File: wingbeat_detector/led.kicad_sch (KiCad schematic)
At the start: 7 parts, among them J2 CONN_UMC_JACK_SMD, Q1 MOSFET-N-CH, U6 LED_DRV_50mA

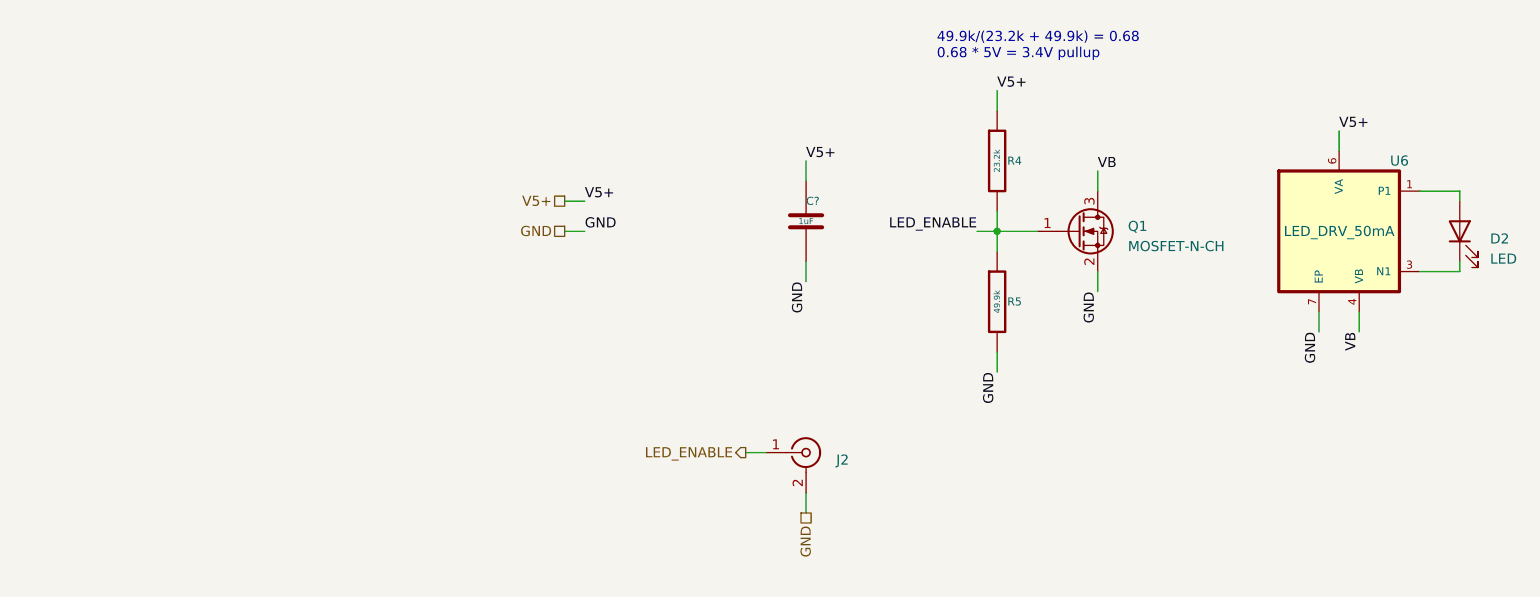
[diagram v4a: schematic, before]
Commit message: Initial schematic layout
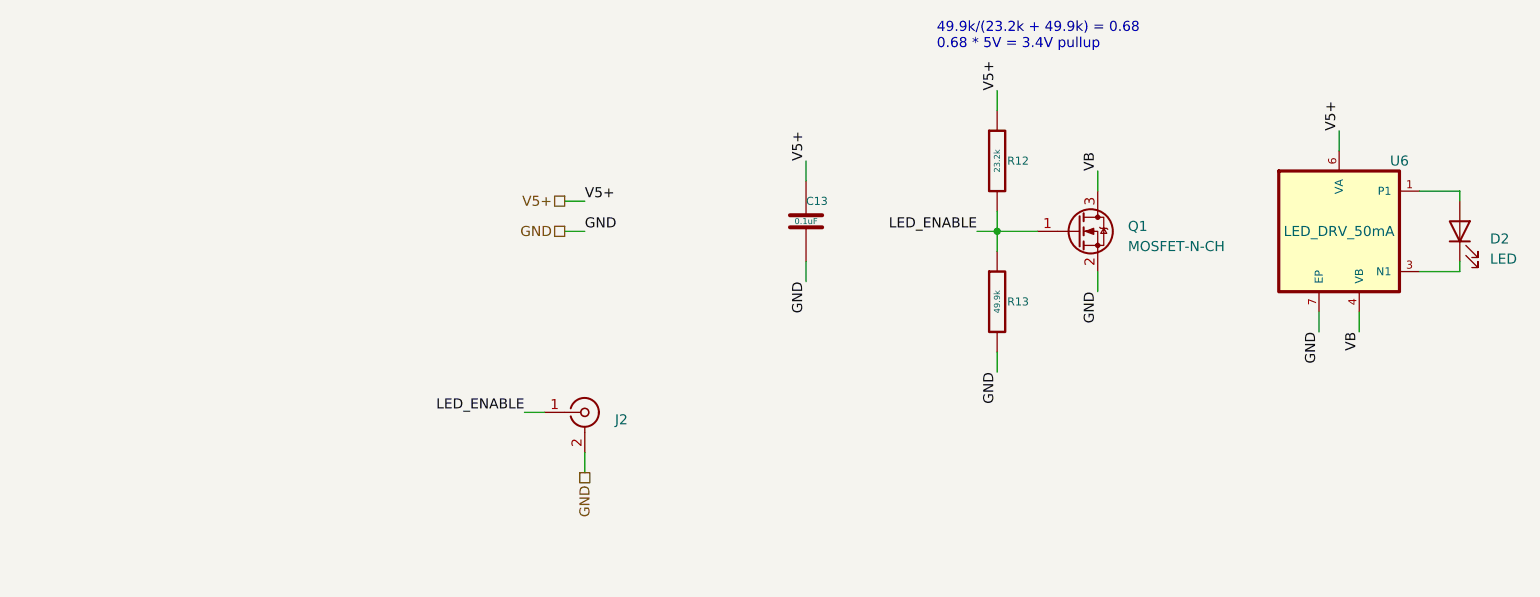
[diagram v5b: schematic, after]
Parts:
- removed C?: 1uF, Janelia:C_0402_1005Metric, symbol Janelia:C_1uF_0402
- added C13: 0.1uF, Janelia:C_0402_1005Metric, symbol Janelia:C_0.1uF_0402
- renumbered R4 to R12, R5 to R13
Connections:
- net GND: now also C13.2
- net V5+: now also C13.1
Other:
- moved on the sheet: J2
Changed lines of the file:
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@@
     (stroke (width 0) (type default))
   )
-  (wire (pts (xy 132.08 121.92) (xy 132.08 124.46))
+  (wire (pts (xy 104.14 116.84) (xy 104.14 119.38))
     (stroke (width 0) (type default))
   )
@@
     (stroke (width 0) (type default))
   )
-  (wire (pts (xy 124.46 116.84) (xy 127 116.84))
+  (wire (pts (xy 96.52 111.76) (xy 99.06 111.76))
     (stroke (width 0) (type default))
   )
@@
   )
   (text "49.9k/(23.2k + 49.9k) = 0.68\n0.68 * 5V = 3.4V pullup"
-    (at 148.59 67.31 0)
-    (effects (font (size 1.27 1.27)) (justify left bottom))
-  )
-  (label "V5+" (at 156.21 71.12 0) (fields_autoplaced)
-    (effects (font (size 1.27 1.27)) (justify left bottom))
-  )
-  (label "V5+" (at 199.39 76.2 0) (fields_autoplaced)
+    (at 148.59 66.04 0)
+    (effects (font (size 1.27 1.27)) (justify left bottom))
+  )
+  (label "V5+" (at 156.21 71.12 90) (fields_autoplaced)
+    (effects (font (size 1.27 1.27)) (justify left bottom))
+  )
+  (label "V5+" (at 199.39 76.2 90) (fields_autoplaced)
     (effects (font (size 1.27 1.27)) (justify left bottom))
   )
@@
     (effects (font (size 1.27 1.27)) (justify right bottom))
   )
+  (label "LED_ENABLE" (at 96.52 111.76 180) (fields_autoplaced)
+    (effects (font (size 1.27 1.27)) (justify right bottom))
+  )
   (label "GND" (at 156.21 106.68 270) (fields_autoplaced)
     (effects (font (size 1.27 1.27)) (justify right bottom))
@@
     (effects (font (size 1.27 1.27)) (justify right bottom))
   )
-  (label "VB" (at 168.91 81.28 0) (fields_autoplaced)
-    (effects (font (size 1.27 1.27)) (justify left bottom))
-  )
-  (label "V5+" (at 132.08 80.01 0) (fields_autoplaced)
+  (label "VB" (at 168.91 81.28 90) (fields_autoplaced)
+    (effects (font (size 1.27 1.27)) (justify left bottom))
+  )
+  (label "V5+" (at 132.08 80.01 90) (fields_autoplaced)
     (effects (font (size 1.27 1.27)) (justify left bottom))
   )
@@
     (effects (font (size 1.27 1.27)) (justify right))
   )
-  (hierarchical_label "LED_ENABLE" (shape output) (at 124.46 116.84 180) (fields_autoplaced)
-    (effects (font (size 1.27 1.27)) (justify right))
-  )
   (hierarchical_label "GND" (shape passive) (at 101.6 88.9 180) (fields_autoplaced)
     (effects (font (size 1.27 1.27)) (justify right))
   )
-  (hierarchical_label "GND" (shape passive) (at 132.08 124.46 270) (fields_autoplaced)
+  (hierarchical_label "GND" (shape passive) (at 104.14 119.38 270) (fields_autoplaced)
     (effects (font (size 1.27 1.27)) (justify right))
-  )
-  (symbol (lib_id "Janelia:C_1uF_0402") (at 132.08 87.63 0) (unit 1)
-    (in_bom yes) (on_board yes) (dnp no)
-    (property "Reference" "C?" (at 132.08 85.09 0)
-      (effects (font (size 1.016 1.016)) (justify left))
-    )
-    (property "Value" "1uF" (at 132.08 87.63 0)
-      (effects (font (size 0.762 0.762)))
-    )
-    (property "Footprint" "Janelia:C_0402_1005Metric" (at 133.0452 91.44 0)
-      (effects (font (size 0.762 0.762)) hide)
-    )
-    (property "Datasheet" "" (at 132.08 87.63 0)
-      (effects (font (size 1.524 1.524)) hide)
-    )
-    (property "Vendor" "Digi-Key" (at 134.62 82.55 0)
-      (effects (font (size 1.524 1.524)) hide)
-    )
-    (property "Vendor Part Number" "1276-6796-1-ND" (at 137.16 80.01 0)
-      (effects (font (size 1.524 1.524)) hide)
-    )
-    (property "Description" "CAP CER 1UF 35V X5R" (at 139.7 77.47 0)
-      (effects (font (size 1.524 1.524)) hide)
-    )
-    (property "Package" "0402" (at 132.08 87.63 0)
-      (effects (font (size 1.27 1.27)) hide)
-    )
-    (property "Manufacturer" "Samsung Electro-Mechanics" (at 132.08 87.63 0)
-      (effects (font (size 1.27 1.27)) hide)
-    )
-    (property "Manufacturer Part Number" "CL05A105KL5NRNC" (at 132.08 87.63 0)
-      (effects (font (size 1.27 1.27)) hide)
-    )
-    (pin "1")
-    (pin "2")
-    (instances
-      (project "wingbeat_detector"
-        (path "/cc457ebc-4af6-4663-b19f-8cb38f061cb4/6f9841bf-b0ef-48ff-bf2c-2bd611c72bf3"
-          (reference "C?") (unit 1)
-        )
-        (path "/cc457ebc-4af6-4663-b19f-8cb38f061cb4/669b71f5-24db-4526-af56-a5891b9eda40"
-          (reference "C9") (unit 1)
-        )
-      )
-    )
   )
   (symbol (lib_id "Janelia:R_23.2k_0402") (at 156.21 80.01 0) (unit 1)
     (in_bom yes) (on_board yes) (dnp no)
-    (property "Reference" "R4" (at 157.48 80.01 0)
+    (property "Reference" "R12" (at 157.48 80.01 0)
       (effects (font (size 1.016 1.016)) (justify left))
     )
@@
       (project "wingbeat_detector"
         (path "/cc457ebc-4af6-4663-b19f-8cb38f061cb4/669b71f5-24db-4526-af56-a5891b9eda40"
-          (reference "R4") (unit 1)
+          (reference "R12") (unit 1)
+        )
+      )
+    )
+  )
+  (symbol (lib_id "Janelia:C_0.1uF_0402") (at 132.08 87.63 0) (unit 1)
+    (in_bom yes) (on_board yes) (dnp no)
+    (property "Reference" "C13" (at 132.08 85.09 0)
+      (effects (font (size 1.016 1.016)) (justify left))
+    )
+    (property "Value" "0.1uF" (at 132.08 87.63 0)
+      (effects (font (size 0.762 0.762)))
+    )
+    (property "Footprint" "Janelia:C_0402_1005Metric" (at 133.0452 91.44 0)
+      (effects (font (size 0.762 0.762)) hide)
+    )
+    (property "Datasheet" "" (at 132.08 87.63 0)
+      (effects (font (size 1.524 1.524)) hide)
+    )
+    (property "Vendor" "Digi-Key" (at 134.62 82.55 0)
+      (effects (font (size 1.524 1.524)) hide)
+    )
+    (property "Vendor Part Number" "311-1375-1-ND" (at 137.16 80.01 0)
+      (effects (font (size 1.524 1.524)) hide)
+    )
+    (property "Description" "CAP CER 0.1UF 25V Y5V" (at 139.7 77.47 0)
+      (effects (font (size 1.524 1.524)) hide)
+    )
+    (property "Package" "0402" (at 132.08 87.63 0)
+      (effects (font (size 1.27 1.27)) hide)
+    )
+    (property "Manufacturer" "Yageo" (at 132.08 87.63 0)
+      (effects (font (size 1.27 1.27)) hide)
+    )
+    (property "Manufacturer Part Number" "CC0402ZRY5V8BB104" (at 132.08 87.63 0)
+      (effects (font (size 1.27 1.27)) hide)
+    )
+    (pin "1")
+    (pin "2")
+    (instances
+      (project "wingbeat_detector"
+        (path "/cc457ebc-4af6-4663-b19f-8cb38f061cb4/669b71f5-24db-4526-af56-a5891b9eda40"
+          (reference "C13") (unit 1)
         )
       )
@@
   (symbol (lib_id "Janelia:R_49.9k_0402") (at 156.21 97.79 0) (unit 1)
     (in_bom yes) (on_board yes) (dnp no)
-    (property "Reference" "R5" (at 157.48 97.79 0)
+    (property "Reference" "R13" (at 157.48 97.79 0)
       (effects (font (size 1.016 1.016)) (justify left))
     )
@@
       (project "wingbeat_detector"
         (path "/cc457ebc-4af6-4663-b19f-8cb38f061cb4/669b71f5-24db-4526-af56-a5891b9eda40"
-          (reference "R5") (unit 1)
+          (reference "R13") (unit 1)
         )
       )
     )
   )
-  (symbol (lib_id "Janelia:CONN_UMC_JACK_SMD") (at 132.08 116.84 0) (unit 1)
+  (symbol (lib_id "Janelia:CONN_UMC_JACK_SMD") (at 104.14 111.76 0) (unit 1)
     (in_bom yes) (on_board yes) (dnp no) (fields_autoplaced)
-    (property "Reference" "J2" (at 135.89 117.7682 0)
+    (property "Reference" "J2" (at 107.95 112.6882 0)
       (effects (font (size 1.27 1.27)) (justify left))
     )
-    (property "Value" "CONN_UMC_JACK_SMD" (at 135.001 116.84 90)
-      (effects (font (size 1.27 1.27)) hide)
-    )
-    (property "Footprint" "Janelia:UMC_AMPHENOL_A-1JB" (at 132.08 104.14 0)
-      (effects (font (size 1.27 1.27)) hide)
-    )
-    (property "Datasheet" "" (at 132.08 116.84 0)
-      (effects (font (size 1.27 1.27)) hide)
-    )
-    (property "Manufacturer" "Amphenol RF" (at 132.08 106.68 0)
-      (effects (font (size 1.27 1.27)) hide)
-    )
-    (property "Manufacturer Part Number" "A-1JB" (at 132.08 132.08 0)
-      (effects (font (size 1.27 1.27)) hide)
-    )
-    (property "Vendor" "Digi-Key" (at 132.08 134.62 0)
-      (effects (font (size 1.27 1.27)) hide)
-    )
-    (property "Vendor Part Number" "115-A-1JBCT-ND" (at 132.08 129.54 0)
-      (effects (font (size 1.27 1.27)) hide)
-    )
-    (property "Description" "CONN UMC JACK STR 50 OHM SMD" (at 132.08 101.6 0)
-      (effects (font (size 1.27 1.27)) hide)
-    )
+    (property "Value" "CONN_UMC_JACK_SMD" (at 107.061 111.76 90)
+      (effects (font (size 1.27 1.27)) hide)
+    )
+    (property "Footprint" "Janelia:UMC_AMPHENOL_A-1JB" (at 104.14 99.06 0)
+      (effects (font (size 1.27 1.27)) hide)
+    )
+    (property "Datasheet" "" (at 104.14 111.76 0)
+      (effects (font (size 1.27 1.27)) hide)
+    )
+    (property "Manufacturer" "Amphenol RF" (at 104.14 101.6 0)
+      (effects (font (size 1.27 1.27)) hide)
+    )
+    (property "Manufacturer Part Number" "A-1JB" (at 104.14 127 0)
+      (effects (font (size 1.27 1.27)) hide)
+    )
+    (property "Vendor" "Digi-Key" (at 104.14 129.54 0)
+      (effects (font (size 1.27 1.27)) hide)
+    )
+    (property "Vendor Part Number" "115-A-1JBCT-ND" (at 104.14 124.46 0)
+      (effects (font (size 1.27 1.27)) hide)
+    )
+    (property "Description" "CONN UMC JACK STR 50 OHM SMD" (at 104.14 96.52 0)
+      (effects (font (size 1.27 1.27)) hide)
+    )

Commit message: Double check schematic
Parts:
- renumbered R12 to R15, R13 to R16
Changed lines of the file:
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@@
+    (effects (font (size 1.27 1.27)) (justify right bottom))
+  )
+  (label "GND" (at 104.14 119.38 270) (fields_autoplaced)
     (effects (font (size 1.27 1.27)) (justify right bottom))
   )
@@
     (effects (font (size 1.27 1.27)) (justify right))
   )
-  (hierarchical_label "GND" (shape passive) (at 104.14 119.38 270) (fields_autoplaced)
-    (effects (font (size 1.27 1.27)) (justify right))
-  )
   (symbol (lib_id "Janelia:R_23.2k_0402") (at 156.21 80.01 0) (unit 1)
     (in_bom yes) (on_board yes) (dnp no)
-    (property "Reference" "R12" (at 157.48 80.01 0)
+    (property "Reference" "R15" (at 157.48 80.01 0)
       (effects (font (size 1.016 1.016)) (justify left))
     )
@@
       (project "wingbeat_detector"
         (path "/cc457ebc-4af6-4663-b19f-8cb38f061cb4/669b71f5-24db-4526-af56-a5891b9eda40"
-          (reference "R12") (unit 1)
+          (reference "R15") (unit 1)
         )
       )
@@
   (symbol (lib_id "Janelia:R_49.9k_0402") (at 156.21 97.79 0) (unit 1)
     (in_bom yes) (on_board yes) (dnp no)
-    (property "Reference" "R13" (at 157.48 97.79 0)
+    (property "Reference" "R16" (at 157.48 97.79 0)
       (effects (font (size 1.016 1.016)) (justify left))
     )
@@
       (project "wingbeat_detector"
         (path "/cc457ebc-4af6-4663-b19f-8cb38f061cb4/669b71f5-24db-4526-af56-a5891b9eda40"
-          (reference "R13") (unit 1)
+          (reference "R16") (unit 1)
         )
       )

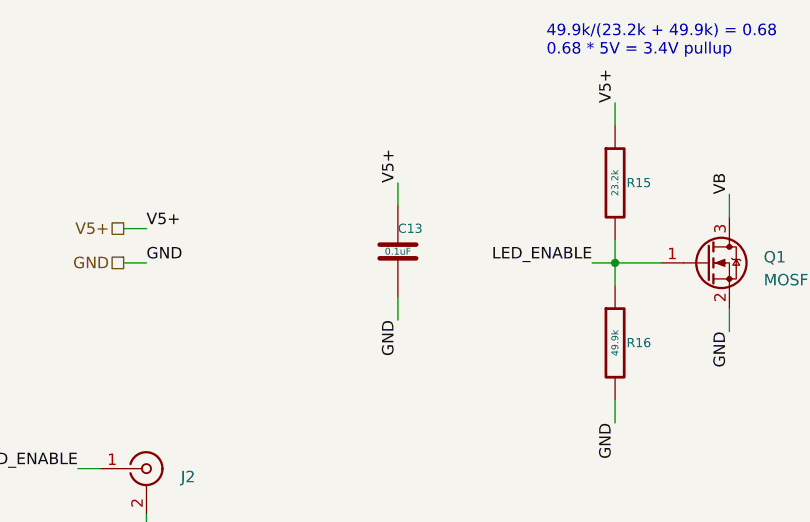
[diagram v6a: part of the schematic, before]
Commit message: Rearrange pcb footprints
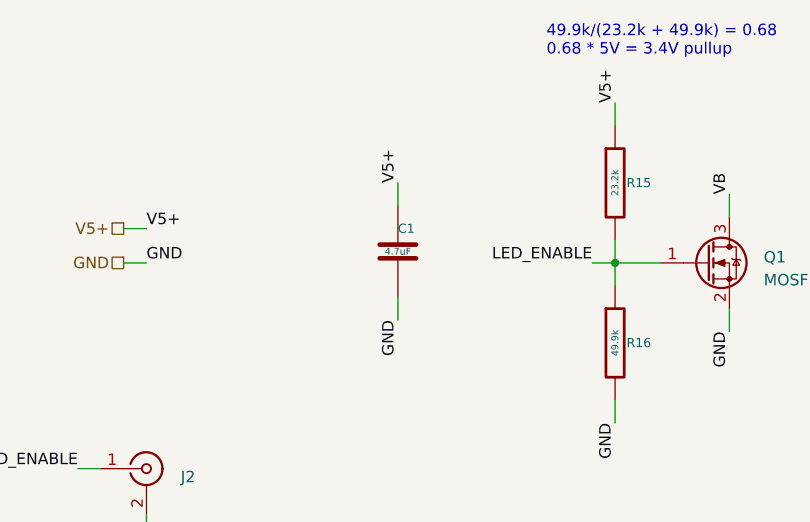
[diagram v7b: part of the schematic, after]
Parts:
- removed C13: 0.1uF, Janelia:C_0402_1005Metric, symbol Janelia:C_0.1uF_0402
- added C1: 4.7uF, Janelia:C_0603_1608Metric, symbol Janelia:C_4.7uF_0603
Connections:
- net GND: now also C1.2
- net V5+: now also C1.1
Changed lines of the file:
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@@
   (title_block
     (title "wingbeat_detector")
+    (date "2023-03-17")
     (rev "3.0")
     (company "Howard Hughes Medical Institute")
@@
     )
   )
-  (symbol (lib_id "Janelia:C_0.1uF_0402") (at 132.08 87.63 0) (unit 1)
+  (symbol (lib_id "Janelia:C_4.7uF_0603") (at 132.08 87.63 0) (unit 1)
     (in_bom yes) (on_board yes) (dnp no)
-    (property "Reference" "C13" (at 132.08 85.09 0)
+    (property "Reference" "C1" (at 132.08 85.09 0)
       (effects (font (size 1.016 1.016)) (justify left))
     )
-    (property "Value" "0.1uF" (at 132.08 87.63 0)
+    (property "Value" "4.7uF" (at 132.08 87.63 0)
       (effects (font (size 0.762 0.762)))
     )
-    (property "Footprint" "Janelia:C_0402_1005Metric" (at 133.0452 91.44 0)
+    (property "Footprint" "Janelia:C_0603_1608Metric" (at 133.0452 91.44 0)
       (effects (font (size 0.762 0.762)) hide)
     )
     (property "Datasheet" "" (at 132.08 87.63 0)
-      (effects (font (size 1.524 1.524)) hide)
+      (effects (font (size 1.524 1.524)))
     )
     (property "Vendor" "Digi-Key" (at 134.62 82.55 0)
       (effects (font (size 1.524 1.524)) hide)
     )
-    (property "Vendor Part Number" "311-1375-1-ND" (at 137.16 80.01 0)
-      (effects (font (size 1.524 1.524)) hide)
-    )
-    (property "Description" "CAP CER 0.1UF 25V Y5V" (at 139.7 77.47 0)
-      (effects (font (size 1.524 1.524)) hide)
-    )
-    (property "Package" "0402" (at 132.08 87.63 0)
-      (effects (font (size 1.27 1.27)) hide)
-    )
-    (property "Manufacturer" "Yageo" (at 132.08 87.63 0)
-      (effects (font (size 1.27 1.27)) hide)
-    )
-    (property "Manufacturer Part Number" "CC0402ZRY5V8BB104" (at 132.08 87.63 0)
-      (effects (font (size 1.27 1.27)) hide)
+    (property "Vendor Part Number" "445-7478-1-ND" (at 137.16 80.01 0)
+      (effects (font (size 1.524 1.524)) hide)
+    )
+    (property "Description" "CAP CER 4.7UF 16V X5R 0603" (at 139.7 77.47 0)
+      (effects (font (size 1.524 1.524)) hide)
+    )
+    (property "Package" "" (at 132.08 87.63 0)
+      (effects (font (size 1.524 1.524)) hide)
+    )
+    (property "Manufacturer" "TDK Corporation" (at 132.08 87.63 0)
+      (effects (font (size 1.524 1.524)) hide)
+    )
+    (property "Manufacturer Part Number" "C1608X5R1C475K080AC" (at 132.08 87.63 0)
+      (effects (font (size 1.524 1.524)) hide)
     )
     (pin "1")
@@
     (instances
       (project "wingbeat_detector"
+        (path "/cc457ebc-4af6-4663-b19f-8cb38f061cb4/6d9b1002-85b6-4eae-b3fb-51bf0c35118b"
+          (reference "C1") (unit 1)
+        )
         (path "/cc457ebc-4af6-4663-b19f-8cb38f061cb4/669b71f5-24db-4526-af56-a5891b9eda40"
           (reference "C13") (unit 1)
